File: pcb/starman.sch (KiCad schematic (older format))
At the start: 25 parts, among them J1 Barrel_Jack_MountingPin, J2 Conn_02x09_Odd_Even, J3 Conn_02x09_Odd_Even, J4 Conn_02x03_Odd_Even, J5 Conn_01x06, SW1 SW_SPST, SW2 SW_Push, U1 LF50_TO220, U2 LF33_TO220

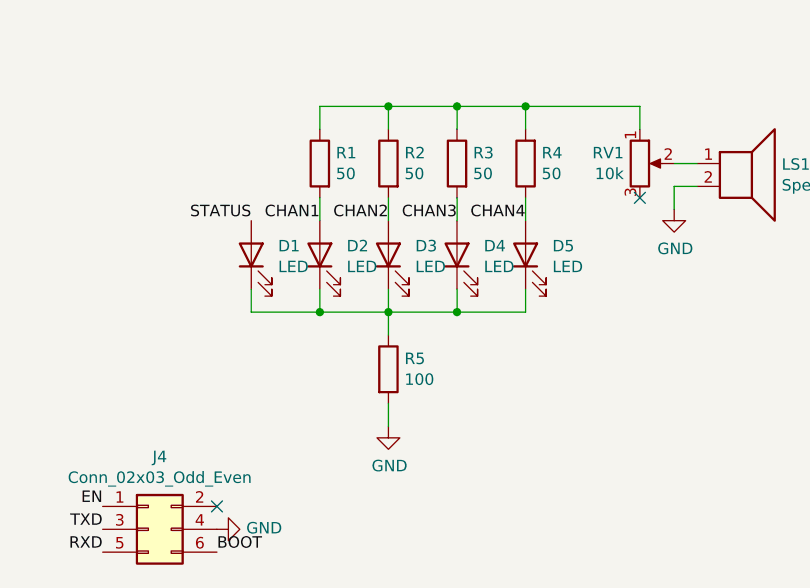
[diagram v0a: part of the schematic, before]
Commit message: Minor adjustments to resistors and some placements
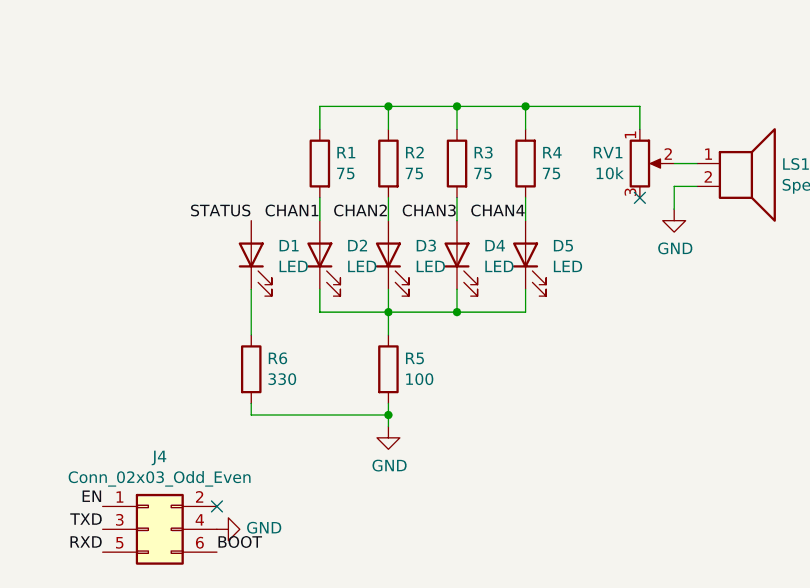
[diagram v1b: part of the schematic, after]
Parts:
- added R6: 330, Resistor_THT:R_Axial_DIN0204_L3.6mm_D1.6mm_P7.62mm_Horizontal, symbol Device:R
- R1, R2, R3, R4: value 50 -> 75
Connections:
- net GND: now also R6.2
- net at D2.1 (K), D3.1 (K), D4.1 (K)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: no longer D1.1 (K)
- new net: D1.1 (K), R6.1
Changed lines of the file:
@@
 P 6650 1750
 F 0 "R2" H 6580 1796 50  0000 R CNN
-F 1 "50" H 6580 1705 50  0000 R CNN
+F 1 "75" H 6580 1705 50  0000 R CNN
 F 2 "Resistor_THT:R_Axial_DIN0204_L3.6mm_D1.6mm_P7.62mm_Horizontal" V 6580 1750 50  0001 C CNN
 F 3 "~" H 6650 1750 50  0001 C CNN
@@
 P 6950 1750
 F 0 "R3" H 6880 1796 50  0000 R CNN
-F 1 "50" H 6880 1705 50  0000 R CNN
+F 1 "75" H 6880 1705 50  0000 R CNN
 F 2 "Resistor_THT:R_Axial_DIN0204_L3.6mm_D1.6mm_P7.62mm_Horizontal" V 6880 1750 50  0001 C CNN
 F 3 "~" H 6950 1750 50  0001 C CNN
@@
 P 7250 1750
 F 0 "R4" H 7180 1704 50  0000 R CNN
-F 1 "50" H 7180 1795 50  0000 R CNN
+F 1 "75" H 7180 1795 50  0000 R CNN
 F 2 "Resistor_THT:R_Axial_DIN0204_L3.6mm_D1.6mm_P7.62mm_Horizontal" V 7180 1750 50  0001 C CNN
 F 3 "~" H 7250 1750 50  0001 C CNN
@@
 P 6350 1750
 F 0 "R1" H 6280 1796 50  0000 R CNN
-F 1 "50" H 6280 1705 50  0000 R CNN
+F 1 "75" H 6280 1705 50  0000 R CNN
 F 2 "Resistor_THT:R_Axial_DIN0204_L3.6mm_D1.6mm_P7.62mm_Horizontal" V 6280 1750 50  0001 C CNN
 F 3 "~" H 6350 1750 50  0001 C CNN
@@
 $EndComp
 Wire Wire Line
-	6050 2300 6050 2400
-Wire Wire Line
-	6050 2400 6350 2400
-Connection ~ 6350 2400
-Wire Wire Line
 	6650 2400 6950 2400
 Wire Wire Line
-	6650 2800 6650 2900
+	6650 2800 6650 2850
 Wire Wire Line
 	6650 2400 6650 2500
@@
 Wire Wire Line
 	4400 1800 4400 1900
+$Comp
+L Device:R R6
+U 1 1 61C9944C
+P 6050 2650
+F 0 "R6" H 6120 2696 50  0000 L CNN
+F 1 "330" H 6120 2605 50  0000 L CNN
+F 2 "Resistor_THT:R_Axial_DIN0204_L3.6mm_D1.6mm_P7.62mm_Horizontal" V 5980 2650 50  0001 C CNN
+F 3 "~" H 6050 2650 50  0001 C CNN
+	1    6050 2650
+	1    0    0    -1
+$EndComp
+Wire Wire Line
+	6050 2300 6050 2500
+Wire Wire Line
+	6050 2800 6050 2850
+Wire Wire Line
+	6050 2850 6650 2850
+Connection ~ 6650 2850
+Wire Wire Line
+	6650 2850 6650 2900
 $EndSCHEMATC
